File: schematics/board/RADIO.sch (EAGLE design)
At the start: 2 parts

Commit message: Платы подготовлены для Резонита
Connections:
- net N$1 renamed GND
- net N$2 renamed 5V
- net N$3 renamed AUX
- net N$4 renamed TXD
- net N$5 renamed RXD
- net N$6 renamed M1
- net N$7 renamed M0
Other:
- moved on the sheet: JP1
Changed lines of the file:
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@@
 <?xml version="1.0" encoding="utf-8"?>
 <!DOCTYPE eagle SYSTEM "eagle.dtd">
-<eagle version="9.6.0">
+<eagle version="9.4.2">
 <drawing>
 <settings>
@@
 <attribute name="NAME" x="5.588" y="31.242" size="1.778" layer="95"/>
 </instance>
-<instance part="JP1" gate="A" x="-15.24" y="20.32" smashed="yes" rot="R180">
-<attribute name="NAME" x="-8.89" y="9.525" size="1.778" layer="95" rot="R180"/>
-<attribute name="VALUE" x="-8.89" y="33.02" size="1.778" layer="96" rot="R180"/>
+<instance part="JP1" gate="A" x="-17.78" y="20.32" smashed="yes" rot="R180">
+<attribute name="NAME" x="-11.43" y="9.525" size="1.778" layer="95" rot="R180"/>
+<attribute name="VALUE" x="-11.43" y="33.02" size="1.778" layer="96" rot="R180"/>
 </instance>
 </instances>
@@
 </busses>
 <nets>
-<net name="N$1" class="0">
+<net name="GND" class="0">
 <segment>
 <pinref part="RADIO" gate="G$1" pin="GND"/>
 <pinref part="JP1" gate="A" pin="1"/>
-<wire x1="-12.7" y1="12.7" x2="0" y2="12.7" width="0.1524" layer="91"/>
+<wire x1="-15.24" y1="12.7" x2="0" y2="12.7" width="0.1524" layer="91"/>
+<label x="-10.16" y="12.7" size="1.778" layer="95"/>
 </segment>
 </net>
-<net name="N$2" class="0">
+<net name="5V" class="0">
 <segment>
 <pinref part="RADIO" gate="G$1" pin="VCC"/>
 <pinref part="JP1" gate="A" pin="2"/>
-<wire x1="-12.7" y1="15.24" x2="0" y2="15.24" width="0.1524" layer="91"/>
+<wire x1="-15.24" y1="15.24" x2="0" y2="15.24" width="0.1524" layer="91"/>
+<label x="-10.16" y="15.24" size="1.778" layer="95"/>
 </segment>
 </net>
-<net name="N$3" class="0">
+<net name="AUX" class="0">
 <segment>
 <pinref part="RADIO" gate="G$1" pin="AUX"/>
 <pinref part="JP1" gate="A" pin="3"/>
-<wire x1="-12.7" y1="17.78" x2="0" y2="17.78" width="0.1524" layer="91"/>
+<wire x1="-15.24" y1="17.78" x2="0" y2="17.78" width="0.1524" layer="91"/>
+<label x="-10.16" y="17.78" size="1.778" layer="95"/>
 </segment>
 </net>
-<net name="N$4" class="0">
+<net name="TXD" class="0">
 <segment>
 <pinref part="RADIO" gate="G$1" pin="TXD"/>
 <pinref part="JP1" gate="A" pin="4"/>
-<wire x1="-12.7" y1="20.32" x2="0" y2="20.32" width="0.1524" layer="91"/>
+<wire x1="-15.24" y1="20.32" x2="0" y2="20.32" width="0.1524" layer="91"/>
+<label x="-10.16" y="20.32" size="1.778" layer="95"/>
 </segment>
 </net>
-<net name="N$5" class="0">
+<net name="RXD" class="0">
 <segment>
 <pinref part="RADIO" gate="G$1" pin="RXD"/>
 <pinref part="JP1" gate="A" pin="5"/>
-<wire x1="-12.7" y1="22.86" x2="0" y2="22.86" width="0.1524" layer="91"/>
+<wire x1="-15.24" y1="22.86" x2="0" y2="22.86" width="0.1524" layer="91"/>
+<label x="-10.16" y="22.86" size="1.778" layer="95"/>
 </segment>
 </net>
-<net name="N$6" class="0">
+<net name="M1" class="0">
 <segment>
 <pinref part="RADIO" gate="G$1" pin="M1"/>
 <pinref part="JP1" gate="A" pin="6"/>
-<wire x1="-12.7" y1="25.4" x2="0" y2="25.4" width="0.1524" layer="91"/>
+<wire x1="-15.24" y1="25.4" x2="0" y2="25.4" width="0.1524" layer="91"/>
+<label x="-10.16" y="25.4" size="1.778" layer="95"/>
 </segment>
 </net>
-<net name="N$7" class="0">
+<net name="M0" class="0">
 <segment>
 <pinref part="RADIO" gate="G$1" pin="M0"/>
 <pinref part="JP1" gate="A" pin="7"/>
-<wire x1="-12.7" y1="27.94" x2="0" y2="27.94" width="0.1524" layer="91"/>
+<wire x1="-15.24" y1="27.94" x2="0" y2="27.94" width="0.1524" layer="91"/>
+<label x="-10.16" y="27.94" size="1.778" layer="95"/>
 </segment>
 </net>

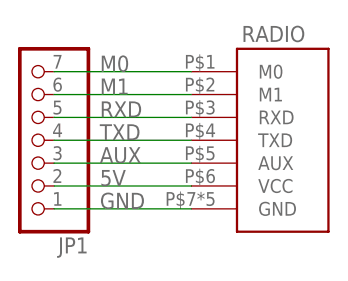
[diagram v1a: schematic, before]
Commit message: Добавлена схема АС, исправлена плата RADIO
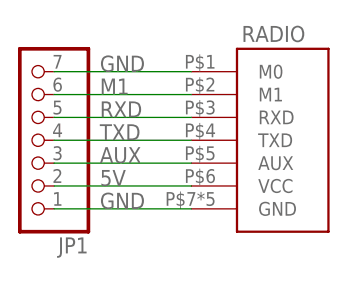
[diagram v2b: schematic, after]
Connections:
- removed net M0: JP1.7, RADIO.M0
- net GND: now also JP1.7, RADIO.M0
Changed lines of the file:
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@@
 <label x="-10.16" y="12.7" size="1.778" layer="95"/>
+</segment>
+<segment>
+<pinref part="RADIO" gate="G$1" pin="M0"/>
+<pinref part="JP1" gate="A" pin="7"/>
+<wire x1="-15.24" y1="27.94" x2="0" y2="27.94" width="0.1524" layer="91"/>
+<label x="-10.16" y="27.94" size="1.778" layer="95"/>
 </segment>
 </net>
@@
 </segment>
 </net>
-<net name="M0" class="0">
-<segment>
-<pinref part="RADIO" gate="G$1" pin="M0"/>
-<pinref part="JP1" gate="A" pin="7"/>
-<wire x1="-15.24" y1="27.94" x2="0" y2="27.94" width="0.1524" layer="91"/>
-<label x="-10.16" y="27.94" size="1.778" layer="95"/>
-</segment>
-</net>
